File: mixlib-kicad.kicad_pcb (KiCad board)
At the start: 2 copper layers, 13 parts, among them Q1 MMBT5551L, Q2 MMBT5551L, Q3 PMD3001D, Q4 PBSS4160DS, Q5 DMC2990UDJQ, Q6 PBSS4160DPN, Q7 DMN3032LFDBQ, U2 MCP6404, U4 LM4040DBZ-10, U5 TPS5430DDA, U6 TJ-S1615CY6TGLCCYRGY-A5

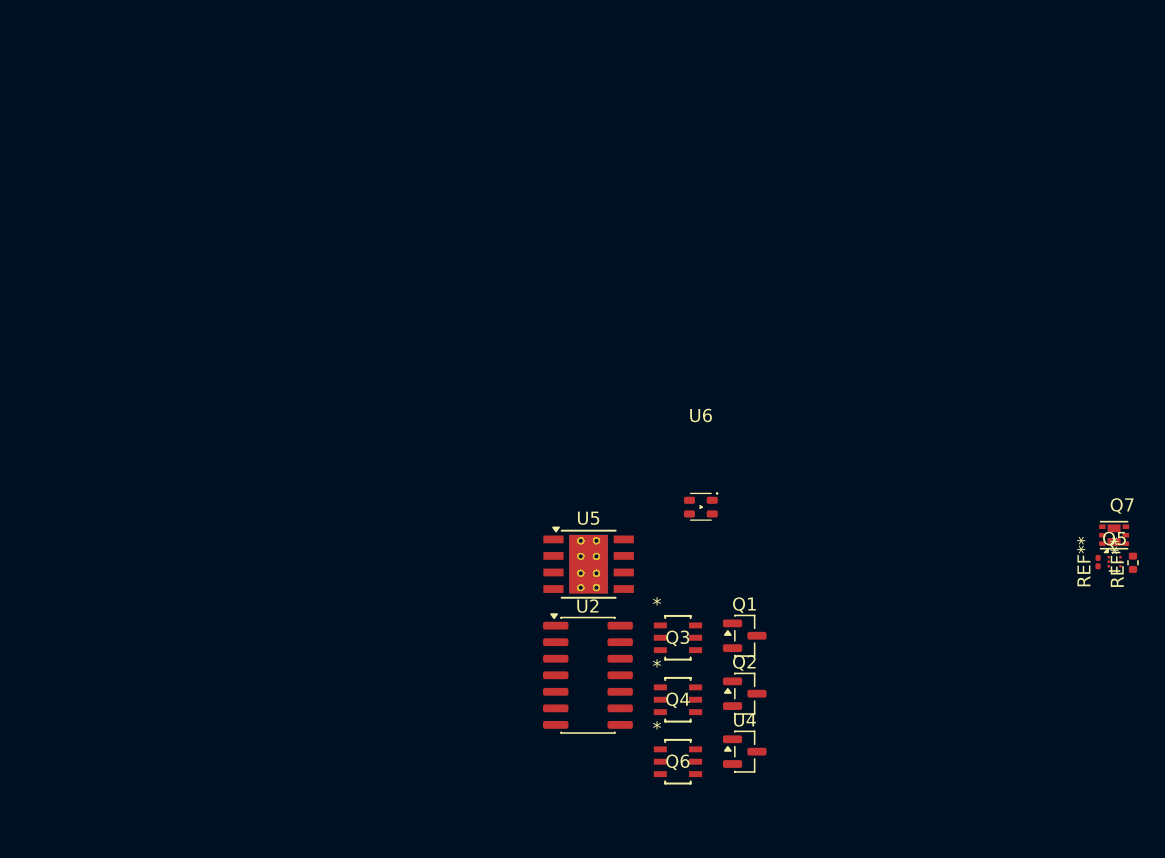
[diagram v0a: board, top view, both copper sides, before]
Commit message: feat(connector-general): add barrel jack connector with 3D model
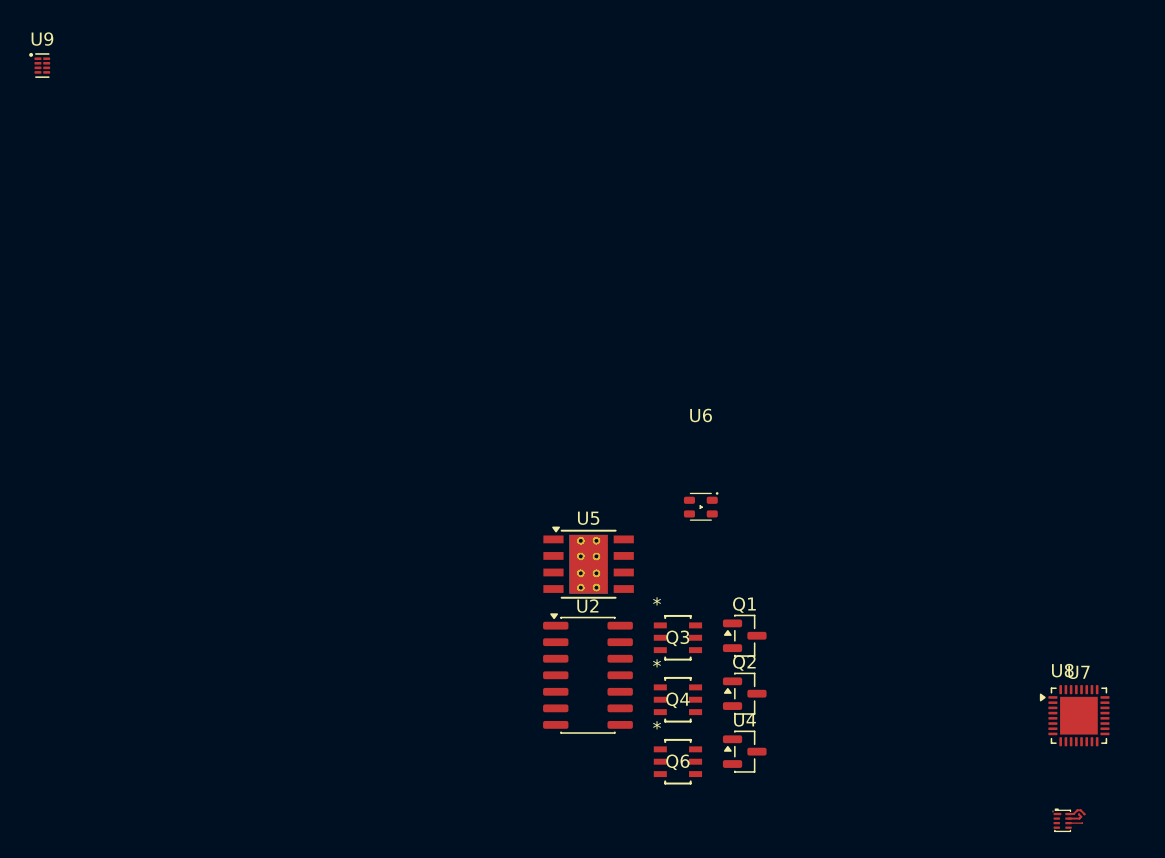
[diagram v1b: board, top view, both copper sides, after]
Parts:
- removed Q5: DMC2990UDJQ, mixlib-generic-sot:SOT-963
- removed Q7: DMN3032LFDBQ, mixlib-generic-dfn:Diodes-Incorporated_U-DFN2020-6_Type-B
- removed REF**: R_0402_1005Metric, Resistor_SMD:R_0402_1005Metric
- removed REF**: R_0201_0603Metric, Resistor_SMD:R_0201_0603Metric
- added U7: CH32V006K8U6, Package_DFN_QFN:QFN-32-1EP_4x4mm_P0.4mm_EP2.9x2.9mm, F.Cu at (80.6, 50.9)
- added U8: TXS0102DQE, mixlib-vendor-ti:vendor-ti-DQE0008A, F.Cu at (79.4, 59.0)
- added U9: TXS0102DQE, Package_SON:X2SON-8_1.4x1mm_P0.35mm, F.Cu at (1.01, 0.97)
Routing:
- net unconnected-(U8-VCCB-Pad8): track 0.00 -> 1.50 mm
- net unconnected-(U8-B1-Pad7): track 0.00 -> 1.31 mm
- net unconnected-(U8-B2-Pad6): track 0.00 -> 1.07 mm
